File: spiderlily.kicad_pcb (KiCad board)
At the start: 2 copper layers, 241.3 x 74.6 mm, 125 parts, among them J2 Conn_01x04_MountingPin, J3 Conn_01x05, SW1 MX_SW_HS, SW10 MX_SW_HS, SW11 MX_SW_HS, SW12 MX_SW_HS, SW13 MX_SW_HS, SW14 MX_SW_HS, SW15 MX_SW_HS, SW16 MX_SW_HS, SW17 MX_SW_HS, SW18 MX_SW_HS, SW19 MX_SW_HS, SW2 MX_SW_HS, SW20 MX_SW_HS, SW21 MX_SW_HS, SW22 MX_SW_HS, SW23 MX_SW_HS, SW24 MX_SW_HS, SW25 MX_SW_HS, SW26 MX_SW_HS, SW27 MX_SW_HS, SW28 MX_SW_HS, SW29 MX_SW_HS, SW3 MX_SW_HS, SW30 MX_SW_HS, SW31 MX_SW_HS, SW32 MX_SW_HS, SW33 MX_SW_HS, SW34 MX_SW_HS, SW35 MX_SW_HS, SW36 MX_SW_HS, SW37 MX_SW_HS, SW38 MX_SW_HS, SW39 MX_SW_HS, SW4 MX_SW_HS, SW40 MX_SW_HS, SW41 MX_SW_HS, SW42 MX_SW_HS, SW43 MX_SW_HS, SW44 MX_SW_HS, SW45 MX_SW_HS, SW46 MX_SW_HS, SW47 MX_SW_HS, SW48 Boot, SW49 RESET, SW5 MX_SW_HS, SW6 MX_SW_HS, SW7 MX_SW_HS, SW8 MX_SW_HS, SW9 MX_SW_HS, U1 XC6206PxxxMR, U3 RP2040, U4 W25Q128JVS, Y1 12MHz

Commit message: few changes
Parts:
- added U2: SRV05-4, PCM_marbastlib-various:SOT-23-6-routable, B.Cu at (84.7, 68.6)
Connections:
- J2 pad MP: unconnected-(J2-MountPin-PadMP) -> GND
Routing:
- net +5V: track 12.1 -> 27.7 mm
- net D+: track 29.5 -> 39.2 mm
- net D-: track 28.8 -> 38.5 mm
- net GND: track 97.5 -> 102.3 mm, vias 26 -> 27
- net row2: track 260.6 -> 263.5 mm
- net col3: track 111.4 -> 112.7 mm

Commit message: parts list, minor changes, logo
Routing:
- net GND: track 102.3 -> 106.5 mm, vias 27 -> 29

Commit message: fixing UDB connection
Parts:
- J2: footprint Connector_Molex:Molex_Pico-EZmate_78171-0004_1x04-1MP_P1.20mm_Vertical -> Connector_JST:JST_SH_BM04B-SRSS-TB_1x04-1MP_P1.00mm_Vertical
- moved J2 22.6 mm to (67.5, 69.2)
- moved C1 4.69 mm to (103.7, 69.3)
- moved C2 4.69 mm to (109.2, 70.9)
- moved C8 4.69 mm to (111.8, 68.3)
- moved U1 4.69 mm to (106.1, 71.6)
- moved U2 3.39 mm to (88.1, 69.3), turned to 0 degrees
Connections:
- U2 pad 1: D+ -> D-
- U2 pad 3: unconnected-(U2-IO2-Pad3) -> D+
- U2 pad 4: unconnected-(U2-IO3-Pad4) -> D+
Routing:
- net row2: track 263.5 -> 285.3 mm
- net col3: track 112.7 -> 103.9 mm
- net +3V3: track 164.9 -> 159.6 mm
- net D+: track 39.2 -> 35.1 mm
- net D-: track 38.5 -> 34.3 mm
- net GND: track 106.5 -> 103.1 mm
- net col4: track 75.5 -> 78.3 mm
- net +5V: track 27.7 -> 30.1 mm, vias 0 -> 2

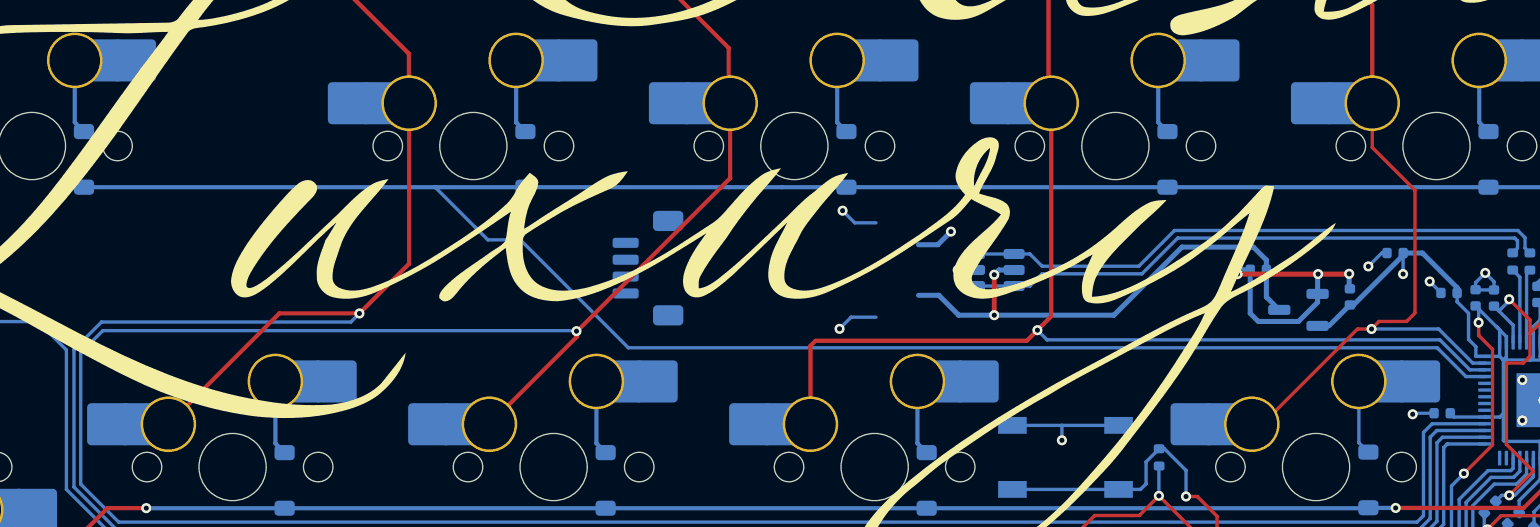
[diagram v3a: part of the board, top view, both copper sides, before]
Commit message: updated ezmate to jst sh, fixed oritentation and clearence issues
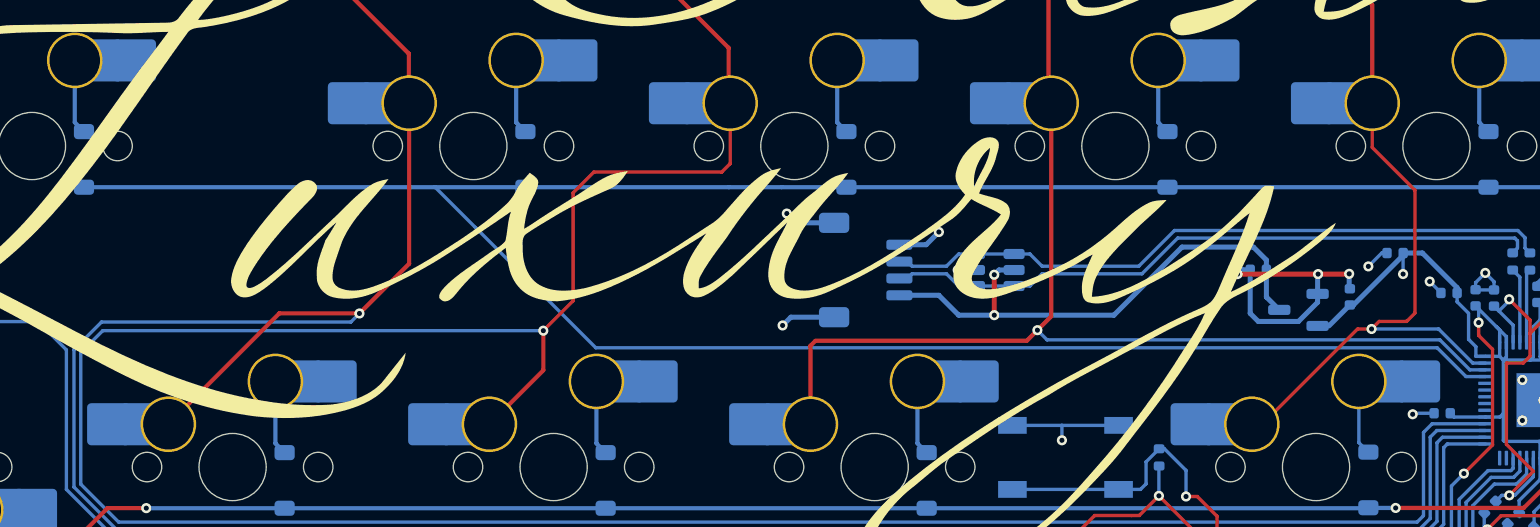
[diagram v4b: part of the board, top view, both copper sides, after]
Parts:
- J2: footprint Connector_JST:JST_SH_BM04B-SRSS-TB_1x04-1MP_P1.00mm_Vertical -> Connector_JST:JST_SH_SM04B-SRSS-TB_1x04-1MP_P1.00mm_Horizontal
- moved J2 12.9 mm to (80.4, 69.3)
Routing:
- net D+: track 35.1 -> 39.9 mm
- net D-: track 34.3 -> 39.2 mm
- net col2: track 196.5 -> 199.0 mm
- net GND: track 103.1 -> 105.0 mm
- net +5V: track 30.1 -> 31.2 mm

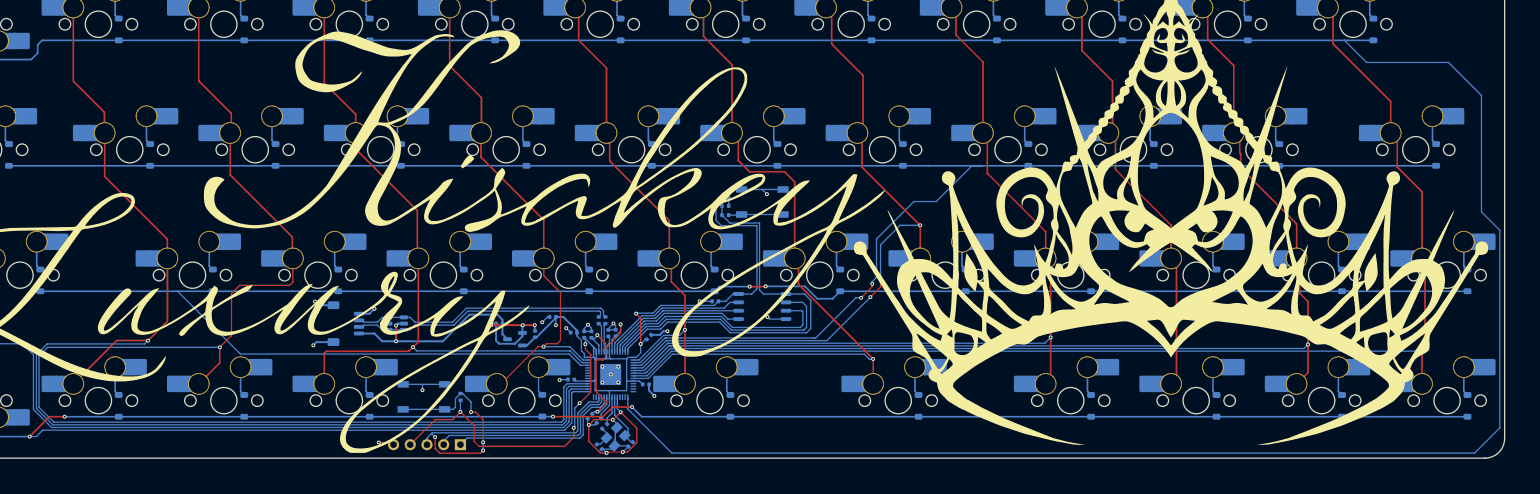
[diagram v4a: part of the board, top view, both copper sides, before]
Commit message: changed trace T angles to triangle polygons, readjusted bottom capacitors to leave 2mm gap from edge of pcb
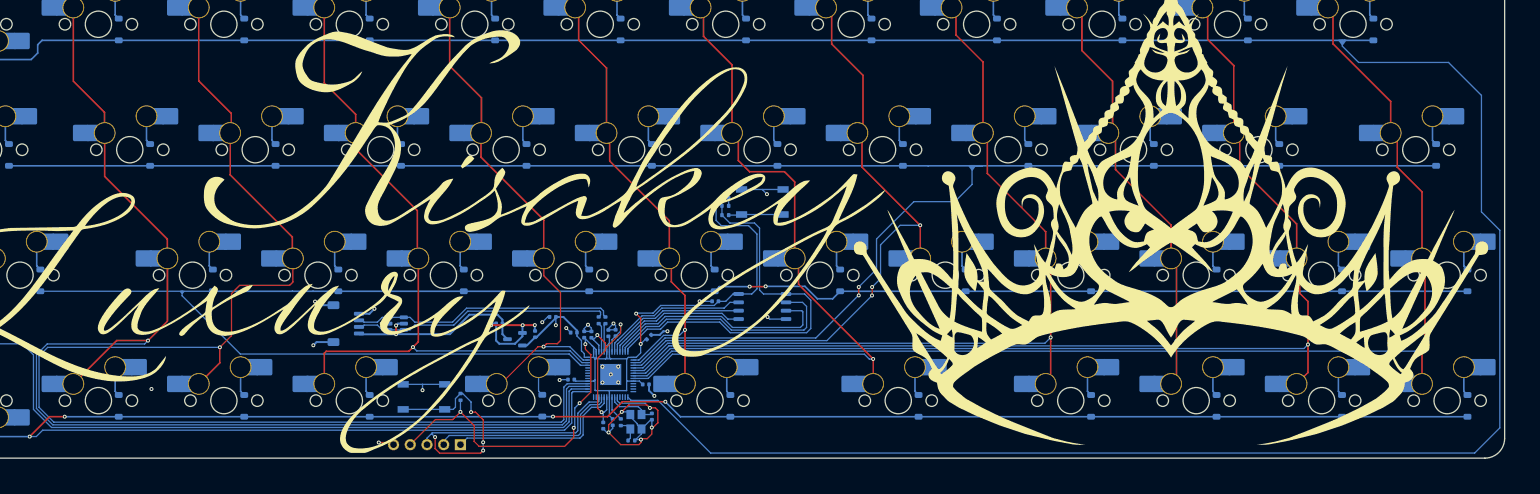
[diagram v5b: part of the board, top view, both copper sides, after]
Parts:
- moved C3 5.31 mm to (126.9, 83.4), turned to 90 degrees
- moved C4 4.98 mm to (123.8, 87.0), turned to 180 degrees
- moved Y1 3.82 mm to (124.5, 84.2), turned to 90 degrees
- moved R7 2.53 mm to (122.2, 84.2), turned to 90 degrees
- moved C7 2.47 mm to (119.5, 84.8), turned to -90 degrees
- moved C16 2.10 mm to (121.0, 84.2), turned to -90 degrees
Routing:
- net GND: track 105.0 -> 108.8 mm, vias 29 -> 30
- net +5V: track 31.2 -> 29.3 mm
- net +1V1: track 31.8 -> 30.8 mm
- net +3V3: track 159.6 -> 158.6 mm
- net row1: track 286.0 -> 287.0 mm
- net XTAL_IN: track 9.22 -> 8.35 mm
- net row3: track 324.8 -> 325.5 mm
- net row0: track 434.0 -> 433.4 mm
- net XTAL_OUT: track 4.39 -> 3.85 mm
